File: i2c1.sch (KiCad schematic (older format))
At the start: 1 part, among them P9 I2C1_0

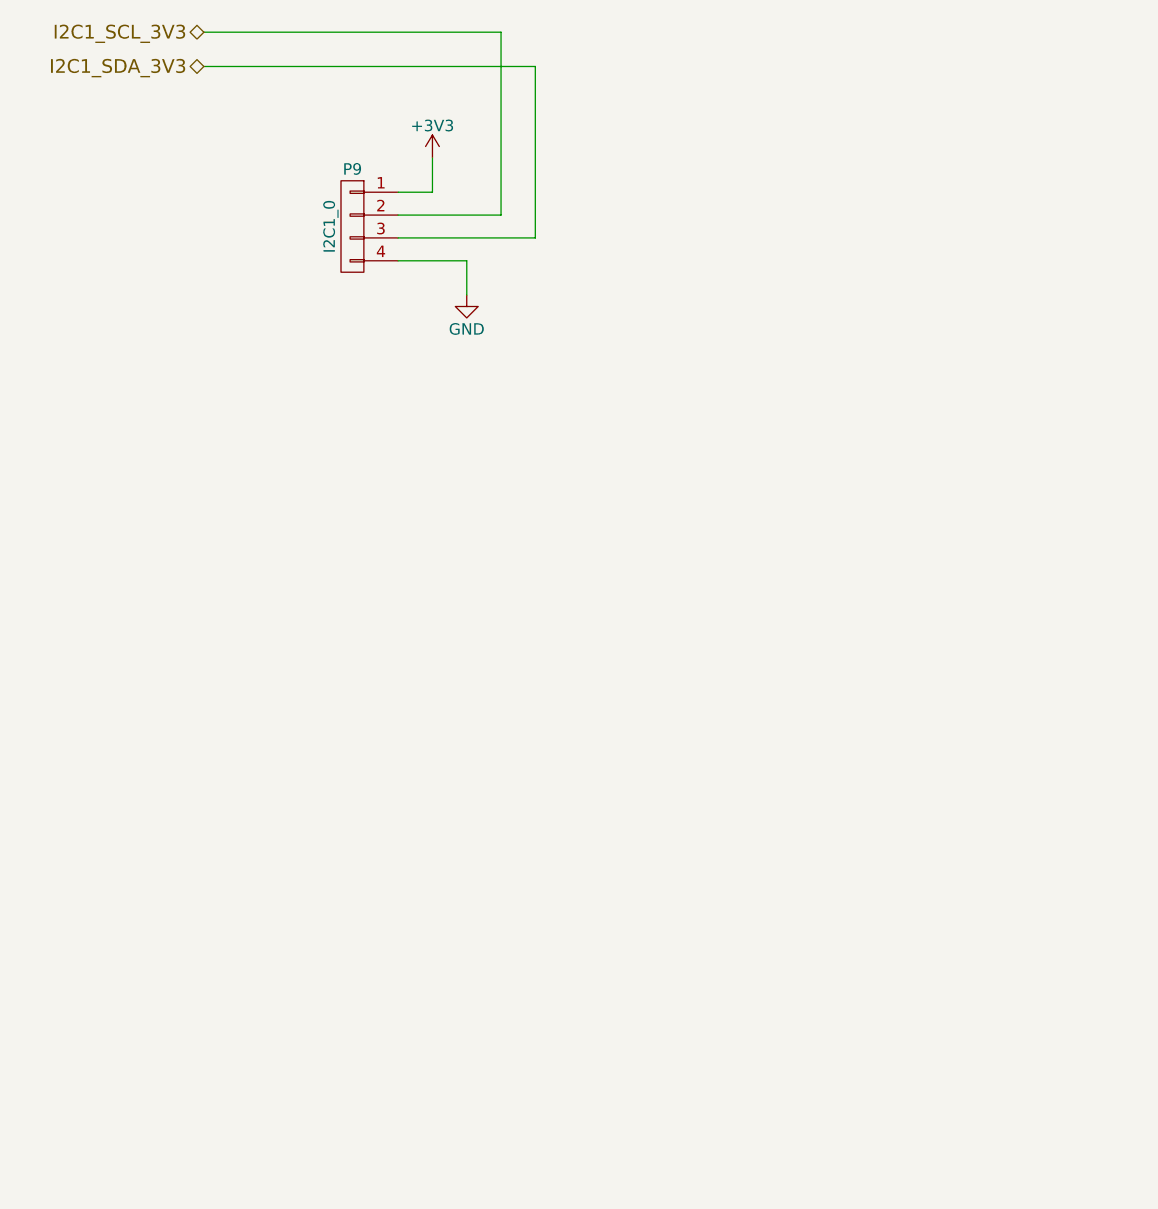
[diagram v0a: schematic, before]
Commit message: Improved the pin comatibility to match with other ardupilot project.
Signed-off-by: Akira Tsukamoto <akira-t@s9.dion.ne.jp>
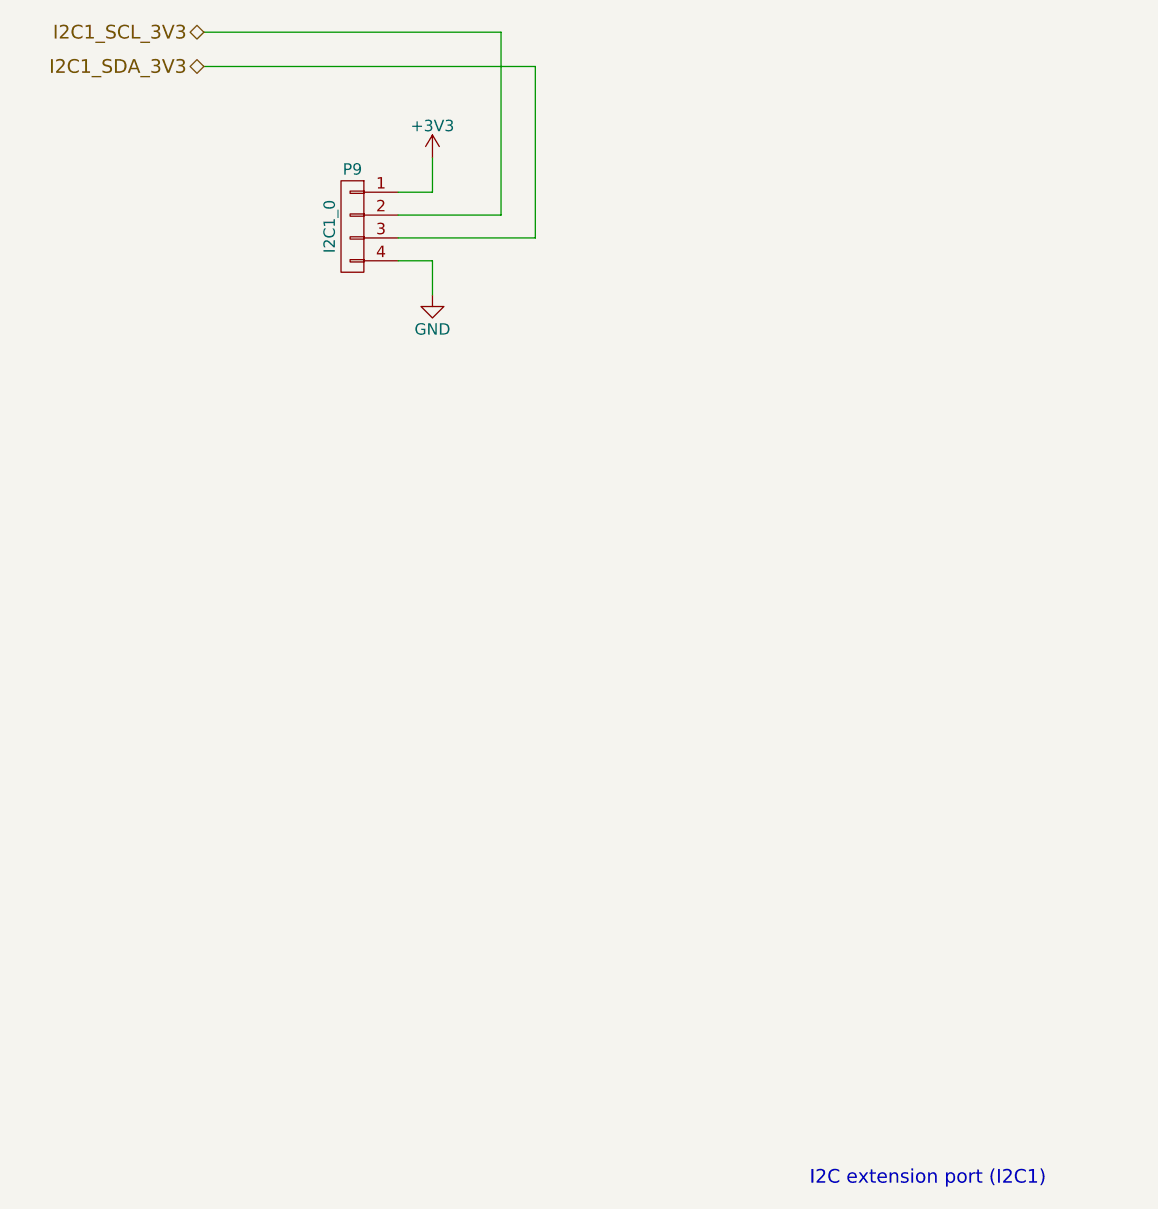
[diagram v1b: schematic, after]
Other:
- note added: "I2C extension port (I2C1)"
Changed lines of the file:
@@
 $EndComp
 $Comp
-L GND #PWR089
+L GND #PWR091
 U 1 1 56F7EFD5
-P 5800 3600
-F 0 "#PWR089" H 5800 3350 50  0001 C CNN
-F 1 "GND" H 5800 3450 50  0000 C CNN
-F 2 "" H 5800 3600 60  0000 C CNN
-F 3 "" H 5800 3600 60  0000 C CNN
-	1    5800 3600
+P 5650 3600
+F 0 "#PWR091" H 5650 3350 50  0001 C CNN
+F 1 "GND" H 5650 3450 50  0000 C CNN
+F 2 "" H 5650 3600 60  0000 C CNN
+F 3 "" H 5650 3600 60  0000 C CNN
+	1    5650 3600
 	-1   0    0    -1
 $EndComp
@@
 	5650 3150 5500 3150
 Wire Wire Line
-	5800 3450 5500 3450
+	5650 3450 5500 3450
 Wire Wire Line
 	5500 3250 5950 3250
 $Comp
-L +3V3 #PWR090
+L +3V3 #PWR092
 U 1 1 5707745E
 P 5650 3000
-F 0 "#PWR090" H 5650 2850 50  0001 C CNN
+F 0 "#PWR092" H 5650 2850 50  0001 C CNN
 F 1 "+3V3" H 5650 3140 50  0000 C CNN
 F 2 "" H 5650 3000 50  0000 C CNN
@@
 	6100 2600 4650 2600
 Wire Wire Line
-	5800 3600 5800 3450
+	5650 3600 5650 3450
 Wire Wire Line
 	5650 3150 5650 3000
@@
 Wire Wire Line
 	6100 2600 6100 3350
+Text Notes 7300 7500 0    60   ~ 0
+I2C extension port (I2C1)
 $EndSCHEMATC
